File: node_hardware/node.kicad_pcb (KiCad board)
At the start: 2 copper layers, 22 parts, among them IC1 bluepill, IC2 Ra-01, IC3 TPS73201, J1 Serial, J2 Sensor1, J3 Sensor2

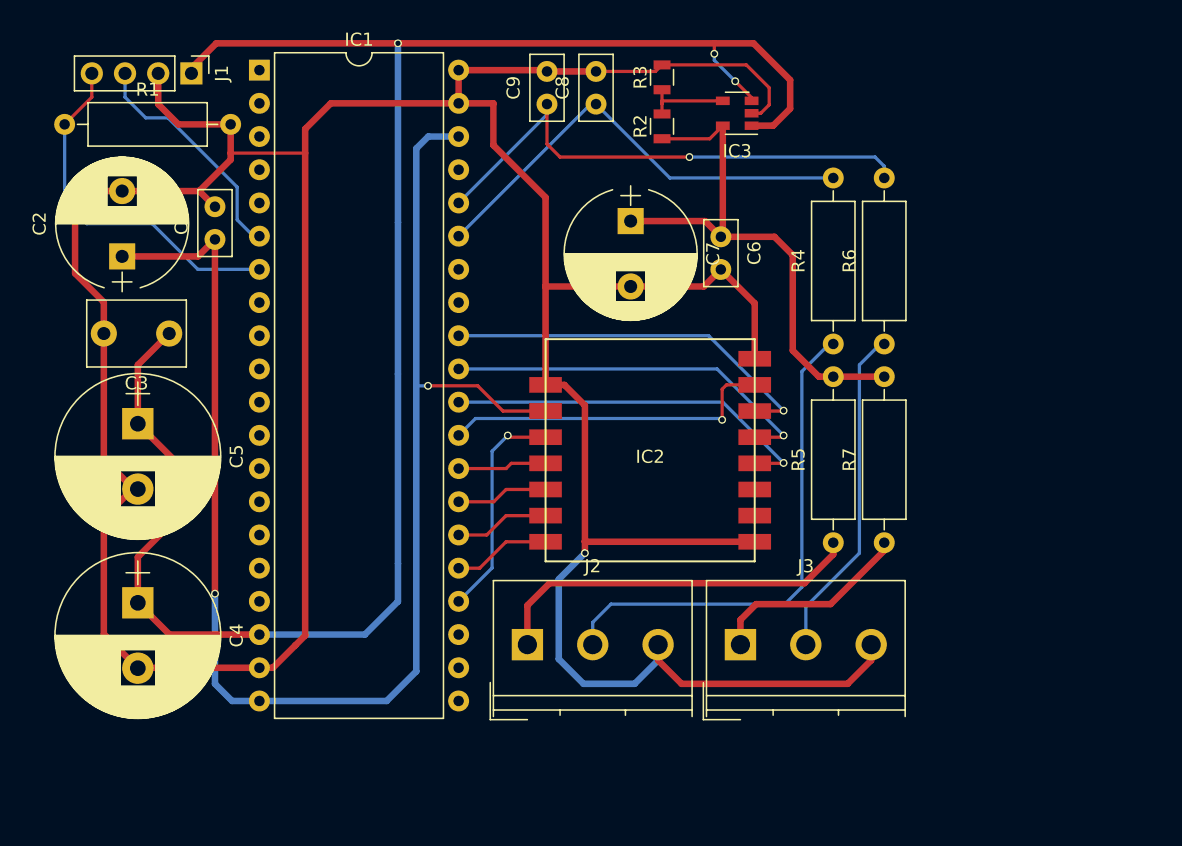
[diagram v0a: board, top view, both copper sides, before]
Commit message: Better Layout + added extension headers
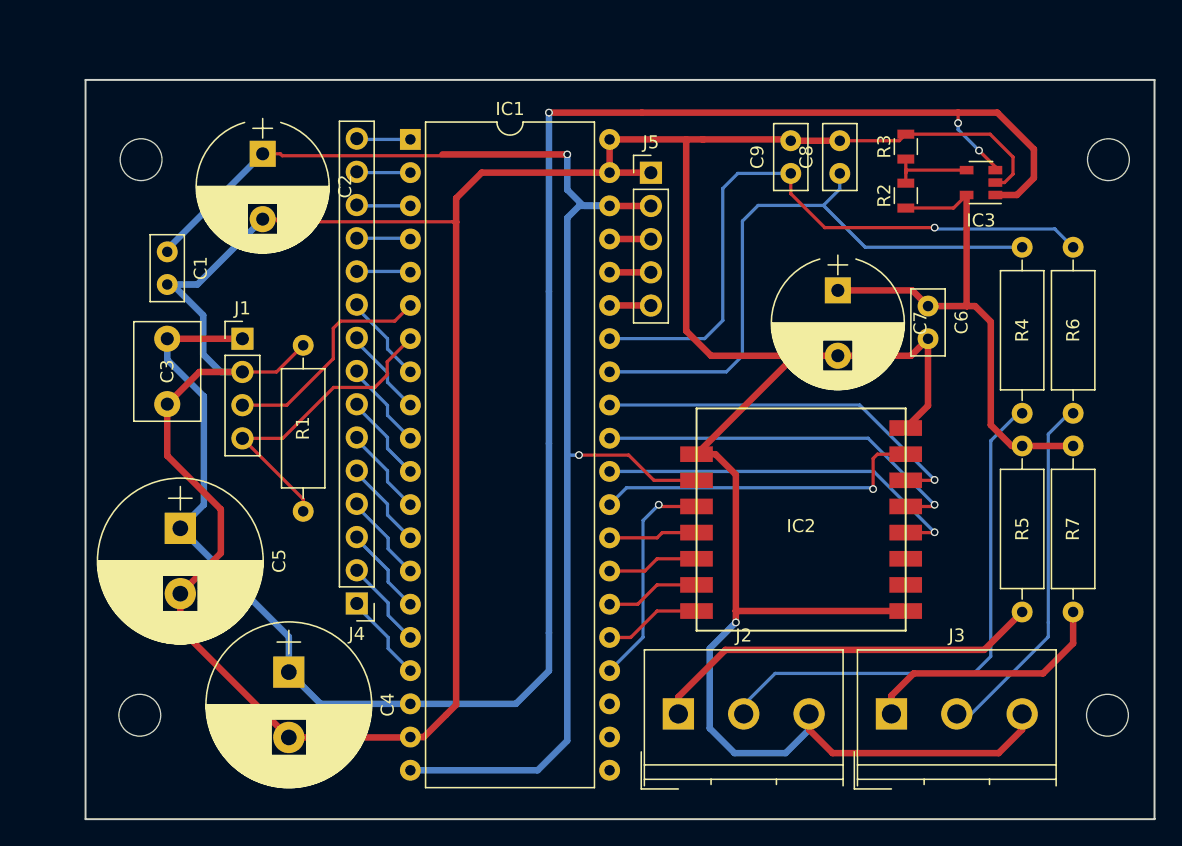
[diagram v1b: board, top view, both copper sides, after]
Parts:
- added ?: MountingHole_3.2mm_M3, Mounting_Holes:MountingHole_3.2mm_M3, F.Cu at (95.5, 24.1)
- added ?: MountingHole_3.2mm_M3, Mounting_Holes:MountingHole_3.2mm_M3, F.Cu at (95.4, 66.6)
- added ?: MountingHole_3.2mm_M3, Mounting_Holes:MountingHole_3.2mm_M3, F.Cu at (21.4, 24.1)
- added ?: MountingHole_3.2mm_M3, Mounting_Holes:MountingHole_3.2mm_M3, F.Cu at (21.4, 66.6)
- added J4: EXT, Pin_Headers:Pin_Header_Straight_1x15_Pitch2.54mm, F.Cu at (38.0, 58.0)
- added J5: EXT2, Pin_Headers:Pin_Header_Straight_1x05_Pitch2.54mm, F.Cu at (60.5, 25.1)
- moved R1 34.8 mm to (33.9, 51.0), turned to 90 degrees
- moved J1 20.7 mm to (29.2, 37.8), turned to 0 degrees
- moved C8 19.4 mm to (74.9, 25.1)
- moved C9 19.4 mm to (71.2, 25.1)
- moved IC3 19.4 mm to (85.7, 25.9)
- moved R2 19.4 mm to (80.0, 26.9)
- moved R3 19.4 mm to (80.0, 23.1)
- moved C6 16.7 mm to (81.7, 35.3)
- moved C7 16.7 mm to (74.8, 34.1)
- moved R7 15.4 mm to (92.8, 58.7)
- moved R6 15.4 mm to (92.8, 43.5)
- moved R5 15.4 mm to (88.8, 58.7)
- moved R4 15.4 mm to (88.8, 43.5)
- moved C2 13.3 mm to (30.8, 23.6), turned to 270 degrees
- moved C4 12.7 mm to (32.8, 63.3)
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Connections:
- IC1 pad 33: Net-(IC1-Pad33) -> Net-(C8-Pad1)
- IC1 pad 34: Net-(IC1-Pad34) -> Net-(C9-Pad1)
- IC1 pad 35: Net-(C8-Pad1) -> Net-(IC1-Pad35)
- IC1 pad 36: Net-(C9-Pad1) -> Net-(IC1-Pad36)
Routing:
- net GND: track 282.3 -> 305.9 mm
- net Net-(C8-Pad1): track 35.2 -> 47.2 mm
- net Net-(C9-Pad1): track 40.8 -> 49.9 mm
- net Net-(IC1-Pad8): track 0.00 -> 7.23 mm
- net Net-(IC1-Pad16): track 0.00 -> 6.94 mm
- net Net-(IC1-Pad17): track 0.00 -> 6.84 mm
- net Net-(IC1-Pad9): track 0.00 -> 6.84 mm
- net Net-(IC1-Pad15): track 0.00 -> 6.84 mm
- net Net-(IC1-Pad14): track 0.00 -> 6.84 mm
- net Net-(IC1-Pad13): track 0.00 -> 6.84 mm
- net Net-(IC1-Pad12): track 0.00 -> 6.84 mm
- net Net-(IC1-Pad11): track 0.00 -> 6.84 mm
- net Net-(IC1-Pad10): track 0.00 -> 6.84 mm
- net Net-(IC1-Pad5): track 0.00 -> 4.14 mm
- net Net-(IC1-Pad1): track 0.00 -> 4.12 mm
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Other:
- board outline added: 81.8 x 56.5 mm
- net class Default: clearance 0.2 -> 0.25
- rule trace_clearance: 0.2 -> 0.25
